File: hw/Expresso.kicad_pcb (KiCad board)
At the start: 4 copper layers, 85.3 x 75.7 mm, 108 parts, among them J1 USB_C_Receptacle_USB2.0_16P, J2 Midi In, J3 Midi Out, J5 Debug, J6 Exp, J7 Exp, J8 Exp, J9 Exp, SW1 Reset, SW2 Boot0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

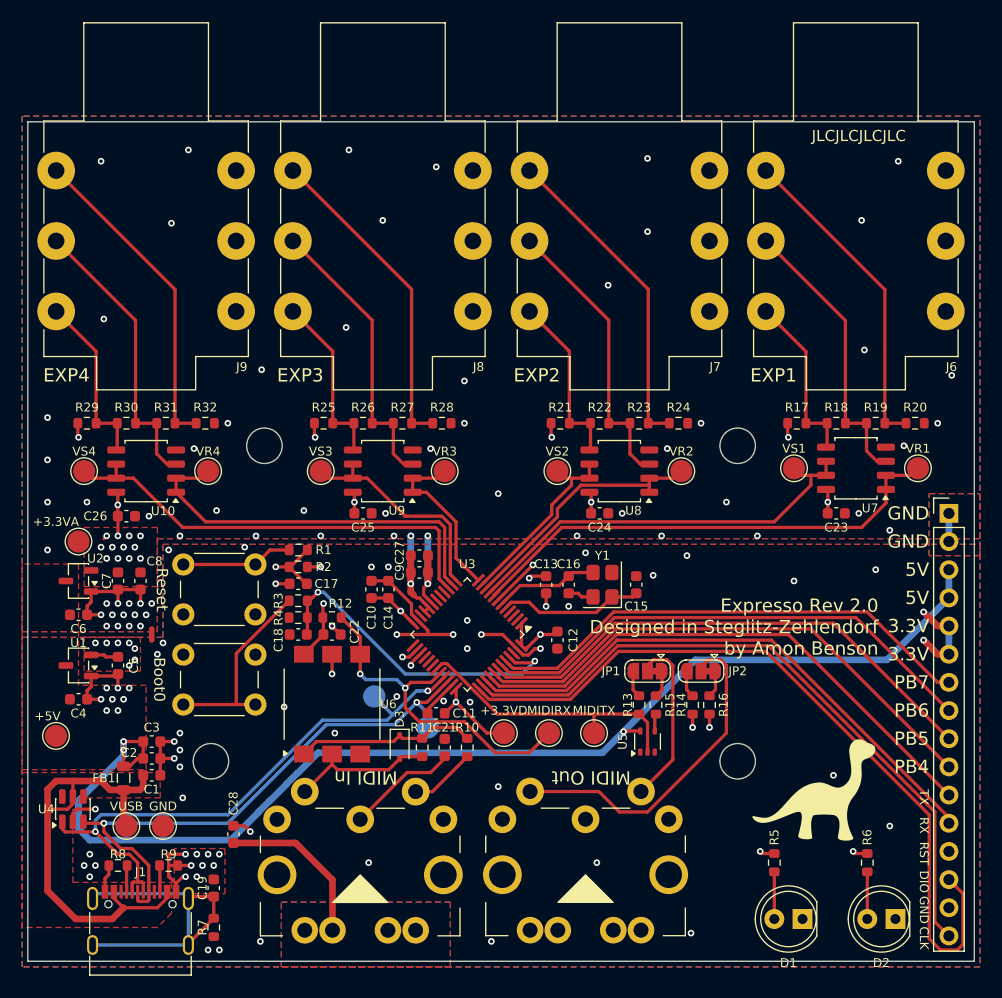
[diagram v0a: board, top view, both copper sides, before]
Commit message: updated connector positions and added new RGB led
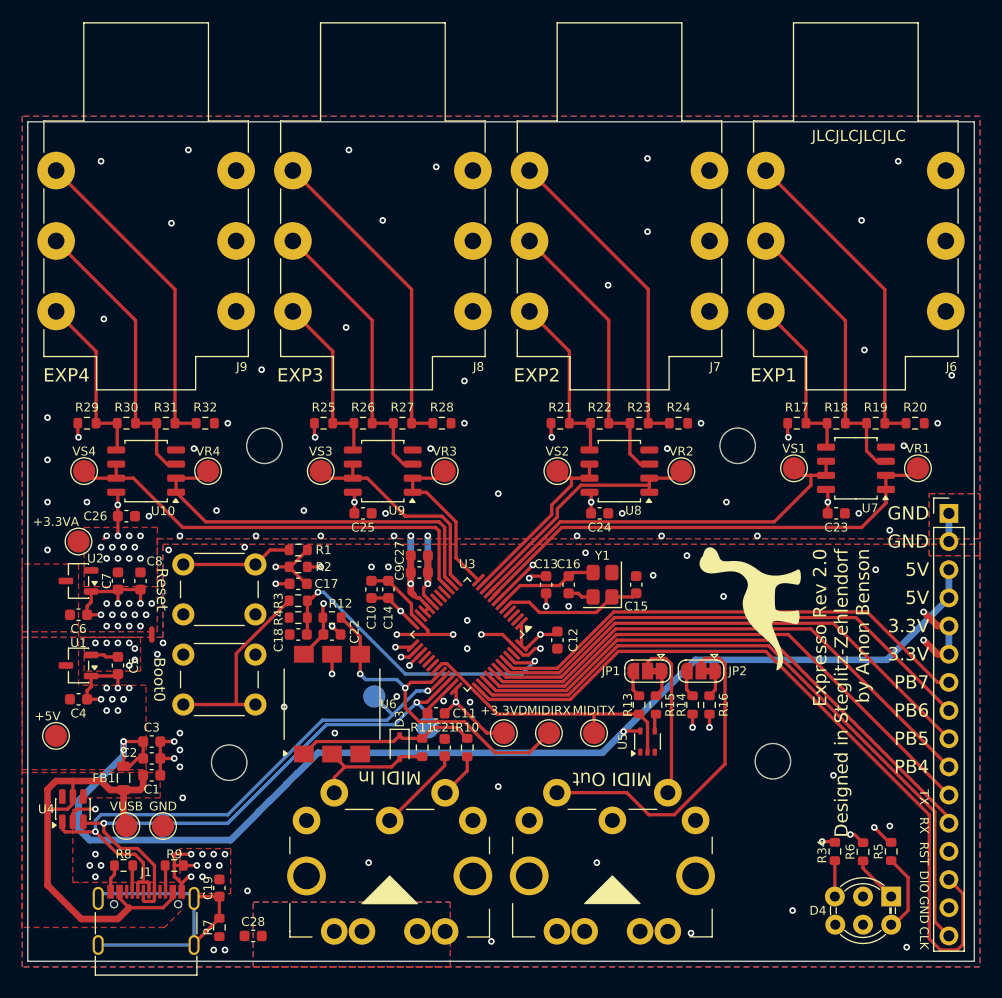
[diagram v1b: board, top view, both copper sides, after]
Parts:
- removed D1, D2: Red, LED_THT:LED_D5.0mm
- added D4: LED_RBK_GBK, LED_THT_6Pin:LED_D5.0mm_6Pin, F.Cu at (198.8, 139.5)
- added R34: 680, Resistor_SMD:R_0603_1608Metric, F.Cu at (196.2, 135.4)
- R6: value 1k -> 2.2k
- moved R5 10.6 mm to (201.3, 135.4), turned to 90 degrees
- moved C28 9.33 mm to (143.8, 143.0), turned to 180 degrees
- moved H1 3.18 mm to (190.6, 127.3)
- moved J2 2.66 mm to (156.1, 132.6)
- moved J3 2.42 mm to (176.2, 132.6)
- moved H2 1.66 mm to (141.6, 127.4)
- moved R6 1.05 mm to (198.8, 135.4)
- moved C19 0.51 mm to (140.7, 138.7)
- moved R7 0.51 mm to (140.7, 142.2)
- moved R8 0.51 mm to (132.1, 136.7)
- moved J1 0.51 mm to (134.1, 142.7)
- moved R9 0.51 mm to (136.7, 136.7)
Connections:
- R5 pad 1: STM_LED1 -> Net-(D4-RA)
- R5 pad 2: Net-(D1-A) -> STM_LED_R
- R6 pad 1: STM_LED2 -> STM_LED_B
- U3 pad 25: unconnected-(U3-PB11-Pad25) -> STM_LED_R
- U3 pad 26: STM_LED1 -> STM_LED_B
- U3 pad 27: STM_LED2 -> STM_LED_G
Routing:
- net STM_LED_R: track 0.00 -> 53.6 mm, vias 0 -> 2
- net STM_LED_B: track 0.00 -> 50.3 mm, vias 0 -> 2
- net STM_LED2: track 49.6 -> 0.00 mm, vias 2 -> 0
- net STM_LED_G: track 0.00 -> 46.5 mm, vias 0 -> 2
- net STM_LED1: track 43.1 -> 0.00 mm, vias 2 -> 0
- net /Midi Connector/MIDI_IN_SHIELD: track 14.9 -> 0.00 mm
- net Net-(D4-RA): track 0.00 -> 7.19 mm
- net Net-(D1-A): track 4.25 -> 0.00 mm
- net Net-(D4-GA): track 0.00 -> 3.24 mm
- net Net-(C21-Pad1): track 9.90 -> 7.86 mm
- net Net-(J2-Pad4): track 5.96 -> 4.08 mm
- net GND: track 63.9 -> 62.1 mm, vias 68 -> 69
- net Net-(D3-A): track 13.2 -> 11.7 mm
- net STM_USB_DM: track 53.3 -> 53.8 mm
- net STM_USB_DP: track 51.8 -> 52.4 mm

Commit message: added new LED traces to hardware
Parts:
- J5: footprint Connector_PinHeader_2.54mm:PinHeader_1x16_P2.54mm_Vertical -> Connector_PinHeader_2.54mm:PinHeader_1x14_P2.54mm_Vertical
- moved J5 33.0 mm to (206.5, 137.9), turned to 180 degrees
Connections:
- J5 pad 1: GND -> STM_SWCLK
- J5 pad 10: STM_SPARE1 -> +3.3V
- J5 pad 11: STM_USART2_TX -> +5V
- J5 pad 12: STM_USART2_RX -> +5V
- J5 pad 13: STM_NRST -> GND
- J5 pad 14: STM_SWDIO -> GND
- J5 pad 3: +5V -> STM_SWDIO
- J5 pad 4: +5V -> STM_NRST
- J5 pad 5: +3.3V -> STM_USART2_RX
- J5 pad 6: +3.3V -> STM_USART2_TX
- J5 pad 7: STM_SPARE4 -> STM_SPARE1
- J5 pad 8: STM_SPARE3 -> STM_SPARE2
- J5 pad 9: STM_SPARE2 -> +3.3V
- U3 pad 16: unconnected-(U3-PB0-Pad16) -> STM_LED_G
- U3 pad 25: STM_LED_R -> unconnected-(U3-PB11-Pad25)
- U3 pad 26: STM_LED_B -> unconnected-(U3-PB12-Pad26)
- U3 pad 27: STM_LED_G -> unconnected-(U3-PB13-Pad27)
- U3 pad 41: STM_SPARE1 -> STM_LED_R
- U3 pad 42: STM_SPARE2 -> STM_LED_B
- U3 pad 43: STM_SPARE3 -> STM_SPARE1
- U3 pad 44: STM_SPARE4 -> STM_SPARE2
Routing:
- net STM_SPARE3: track 46.1 -> 0.00 mm
- net STM_SPARE4: track 45.0 -> 0.00 mm
- net STM_LED_R: track 53.6 -> 42.1 mm
- net STM_LED_B: track 50.3 -> 39.5 mm
- net STM_SWCLK: track 60.9 -> 56.6 mm
- net STM_NRST: track 83.1 -> 79.8 mm
- net STM_SWDIO: track 70.2 -> 67.0 mm
- net STM_SPARE2: track 47.3 -> 45.0 mm
- net STM_SPARE1: track 48.5 -> 46.1 mm
- net STM_USART2_TX: track 49.6 -> 48.3 mm
- net STM_LED_G: track 46.5 -> 45.3 mm
- net STM_USART2_RX: track 50.6 -> 49.5 mm
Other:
- board text removed: "PB4"
- board text removed: "PB5"

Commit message: added final production files for version 2
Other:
- board text removed: "JLCJLCJLCJLC"
